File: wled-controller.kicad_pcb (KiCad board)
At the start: 2 copper layers, 110 x 40 mm, 45 parts, among them J1 Screw_Terminal_01x04, J2 Screw_Terminal_01x06, J3 Conn_01x05_Male, Q1 BC817, SW1 SW_Push, SW2 SW_Push, U1 LM1117-3.3, U2 74HCT00, U3 ESP-07, U4 TSOP45xx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

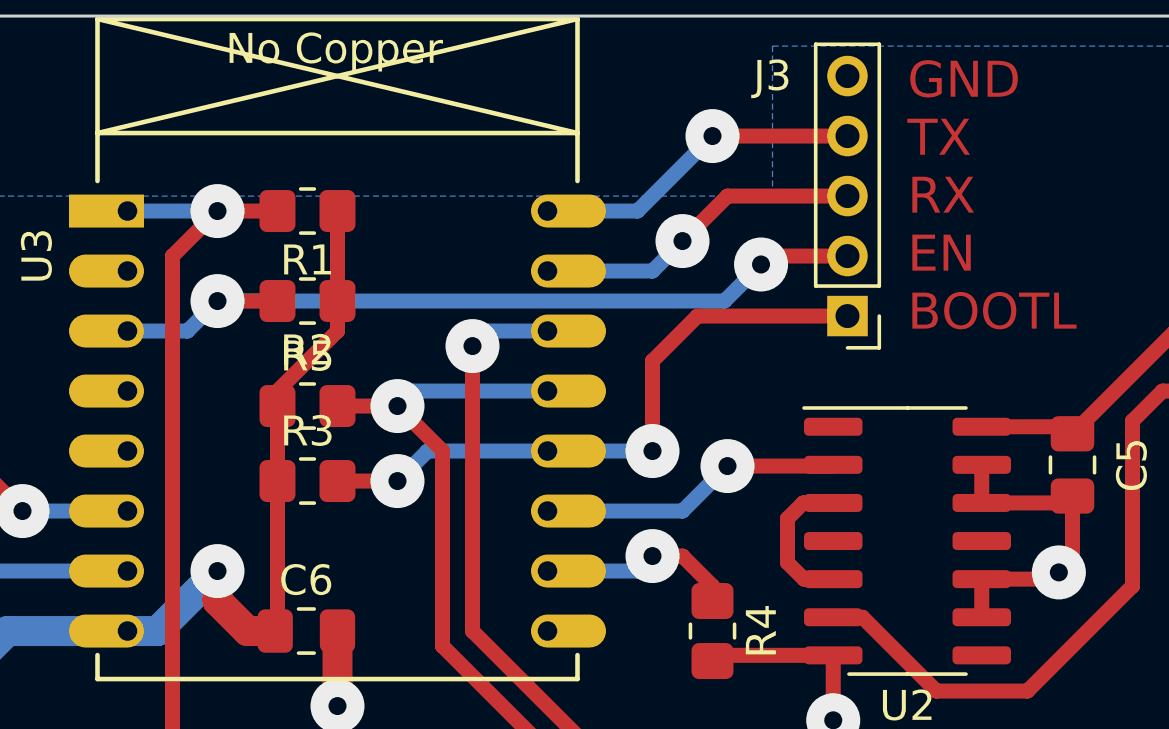
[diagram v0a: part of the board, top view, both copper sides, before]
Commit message: Fix unconnected pad & silkscreen placement
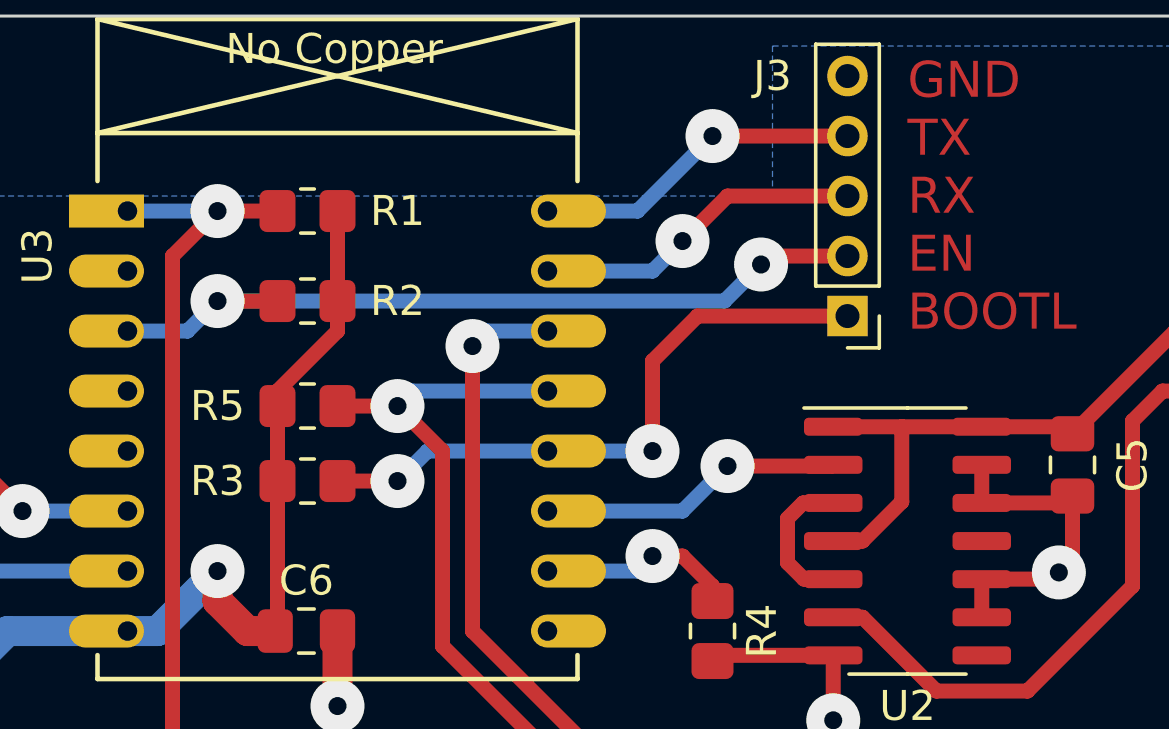
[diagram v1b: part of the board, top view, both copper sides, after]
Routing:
- net +5V: track 221.6 -> 231.9 mm

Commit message: Changed input diode to 1N5817.
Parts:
- D1: value 1N4001 -> 1N5817

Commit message: Minor improvements.
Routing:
- net GND: track 57.8 -> 56.6 mm
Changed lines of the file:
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@@
-(kicad_pcb (version 20171130) (host pcbnew 5.1.10-6.fc33)
+(kicad_pcb (version 20171130) (host pcbnew 5.1.10-6.fc34)
   (general
     (thickness 1.6)
     (drawings 7)
-    (tracks 268)
+    (tracks 267)
     (zones 0)
     (modules 45)
@@
     (47 F.CrtYd user)
     (48 B.Fab user)
-    (49 F.Fab user)
+    (49 F.Fab user hide)
   )
   (setup
@@
   (segment (start 91.41 93.48) (end 91.41 92.5525) (width 1) (layer F.Cu) (net 1) (status 10))
   (segment (start 93.4625 90.4625) (end 93.4625 90.5) (width 1) (layer F.Cu) (net 1) (status 30))
-  (via (at 94.5 86.5) (size 1.8) (drill 0.6) (layers F.Cu B.Cu) (net 1))
-  (segment (start 93.5 90.4625) (end 93.5 87.5) (width 1) (layer F.Cu) (net 1) (status 10))
-  (segment (start 93.5 87.5) (end 94.5 86.5) (width 1) (layer F.Cu) (net 1))
-  (segment (start 93.4625 90.5) (end 93.5 90.4625) (width 1) (layer F.Cu) (net 1) (status 30))
   (segment (start 91.39 93.5) (end 91.41 93.48) (width 1) (layer F.Cu) (net 1) (status 30))
   (segment (start 89 93.5) (end 91.39 93.5) (width 1) (layer F.Cu) (net 1) (status 30))
@@
   (segment (start 118 90.5) (end 118 93) (width 1) (layer F.Cu) (net 1) (status 10))
   (via (at 118 93) (size 1.8) (drill 0.6) (layers F.Cu B.Cu) (net 1))
+  (via (at 94.49999 87.63) (size 1.8) (drill 0.6) (layers F.Cu B.Cu) (net 1))
+  (segment (start 93.4625 90.5) (end 93.4625 88.66749) (width 1) (layer F.Cu) (net 1))
+  (segment (start 93.4625 88.66749) (end 94.49999 87.63) (width 1) (layer F.Cu) (net 1))
   (segment (start 82 86.5) (end 87 86.5) (width 2) (layer B.Cu) (net 2) (status 30))
   (segment (start 81.5 87) (end 82 86.5) (width 1) (layer B.Cu) (net 2) (status 30))

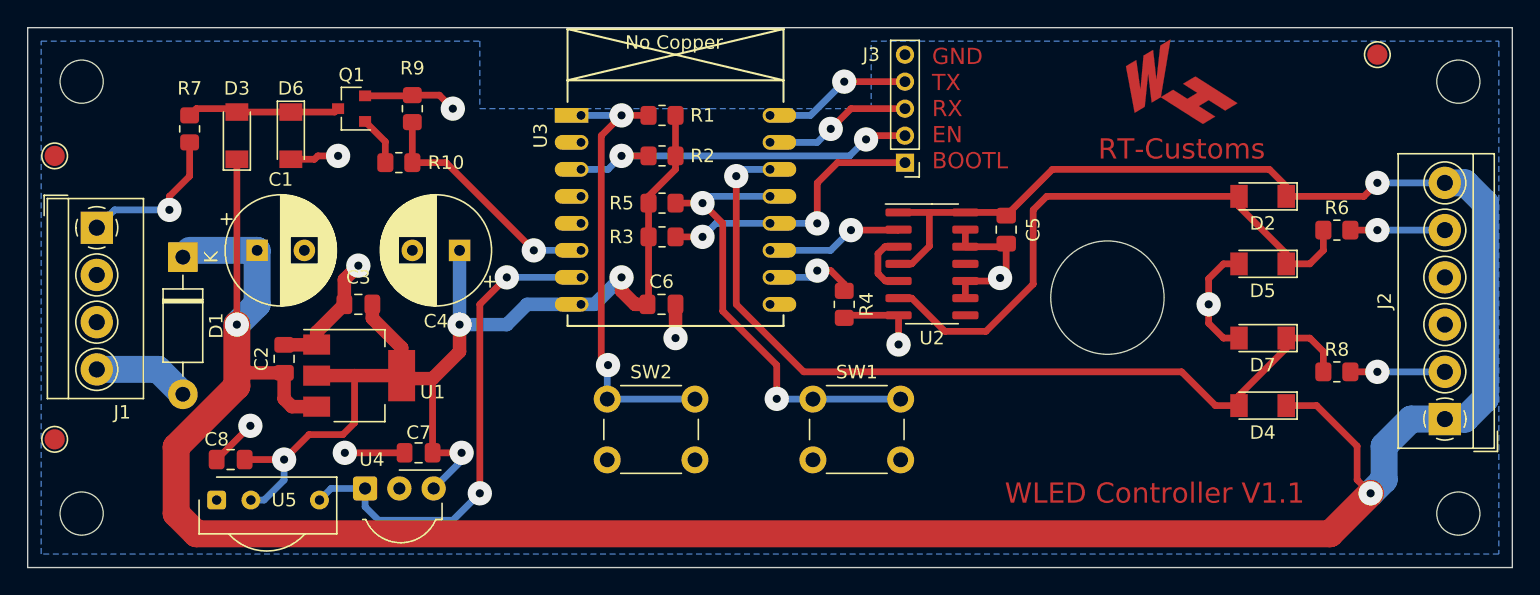
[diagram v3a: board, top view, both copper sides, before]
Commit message: Changed programming header to 2.54mm
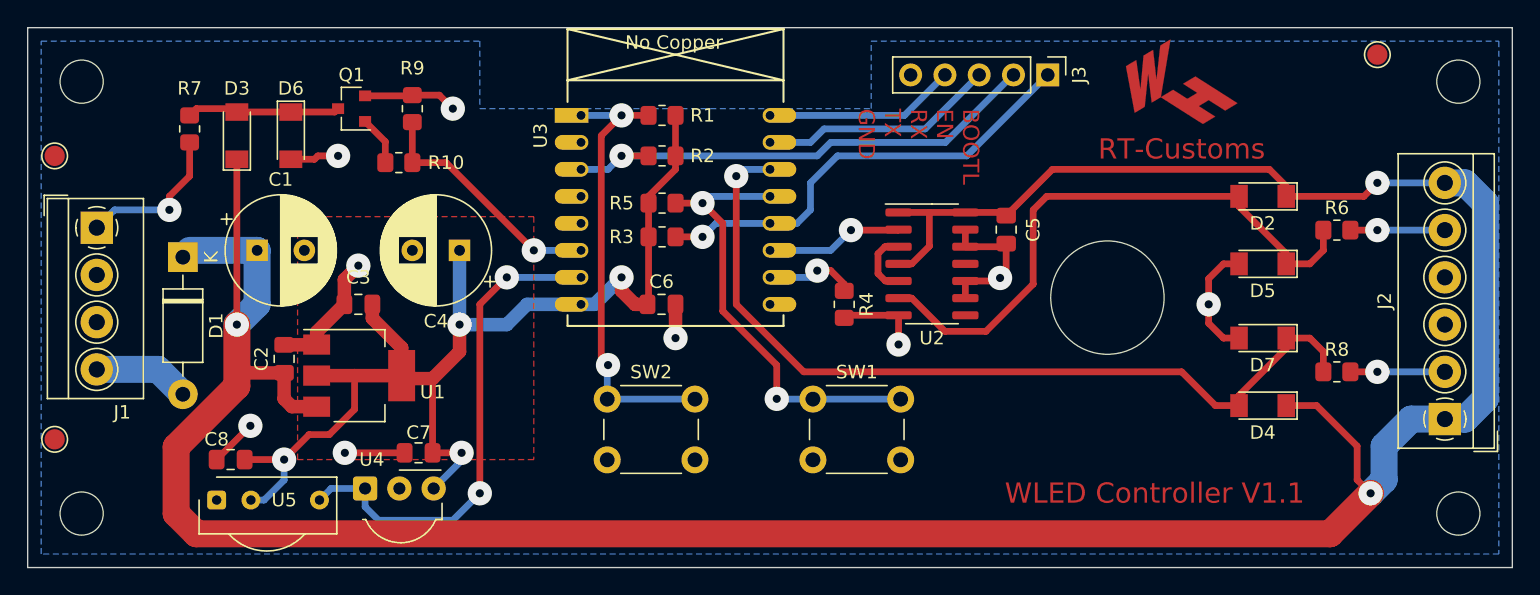
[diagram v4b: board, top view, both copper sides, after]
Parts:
- J3: footprint Connector_PinHeader_2.00mm:PinHeader_1x05_P2.00mm_Vertical -> Connector_PinHeader_2.54mm:PinHeader_1x05_P2.54mm_Vertical
- SW2: footprint Button_Switch_THT:SW_PUSH_6mm_H8mm -> Button_Switch_THT:SW_PUSH_6mm_H13mm
- moved J3 12.4 mm to (145.6, 73.5), turned to 270 degrees
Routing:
- net ESP_BOOTL: track 21.0 -> 33.7 mm, vias 2 -> 1
- net ESP_EN: track 27.0 -> 36.9 mm, vias 2 -> 1
- net ESP_RX: track 11.0 -> 17.6 mm, vias 1 -> 0
- net ESP_TX: track 11.0 -> 14.2 mm, vias 1 -> 0
- net +3V3: track 85.3 -> 84.8 mm
- added copper zone on F.Cu, net +3V3
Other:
- board text added: "BOOTL EN RX TX GND"
- board text removed: "GND TX RX EN BOOTL"

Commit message: Reduced board length to 100mm.
Improved and added Silkscreen features.
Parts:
- moved REF** 47.9 mm to (134.8, 104.5)
- moved G*** 27.4 mm to (146.0, 99.8)
- moved C5 19.7 mm to (158.5, 73.5)
- moved U2 19.7 mm to (153.0, 76.0)
- moved D2 10.0 mm to (151.5, 83.5)
- moved D4 10.0 mm to (151.5, 97.0)
- moved D5 10.0 mm to (151.5, 87.5)
- moved D7 10.0 mm to (151.5, 93.0)
- moved J2 10.0 mm to (165.0, 99.0)
- moved R6 10.0 mm to (157.0, 85.0)
- moved R8 10.0 mm to (157.0, 95.5)
- moved REF** 10.0 mm to (140.0, 90.0)
- moved REF** 10.0 mm to (166.0, 106.0)
- moved REF** 10.0 mm to (166.0, 74.0)
- moved SW1 6.18 mm to (122.0, 97.5)
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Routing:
- net 5V_LED_DATA: track 44.7 -> 19.2 mm
- net ESP_LED_DATA: track 10.2 -> 33.3 mm
- net +5V: track 231.9 -> 209.5 mm
- net ESP_SW2: track 63.7 -> 52.8 mm
- net GND: track 56.6 -> 52.2 mm, vias 9 -> 10
- net ESP_SW1: track 33.2 -> 29.0 mm
- net Net-(R4-Pad1): track 6.62 -> 7.41 mm
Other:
- board size 110 x 40 mm -> 100 x 40 mm
- board text added: "5V DOUT GND GND GPIO 5V"
- board text added: "GND VIN"
- board text added: "PS_ON GND"
- board text added: "WLED Controller V1.2"
- board text removed: "WLED Controller V1.1"
